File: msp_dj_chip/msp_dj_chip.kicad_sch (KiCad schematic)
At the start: 6 parts, among them U1 DAC60502

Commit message: Add files via upload
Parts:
- removed U1: DAC60502, symbol bernie_symbols:DAC
- added C1, C2: 100nF, symbol Device:C_Small
- added C10, C12, C8, C9: 100n, symbol Device:C_Small
- added C11: 4u7, symbol Device:C_Polarized_Small
- added C13: u1F, symbol Device:C_Small
- added C14: 10uF, symbol Device:C_Small
- added C15: u47, symbol Device:C_Small
- added C16: 10nF, symbol Device:C_Small
- added C17, C18: 15pF, symbol Device:C_Small
- added C3: 150nF, symbol Device:C_Small
- added C4, C5: 10u, symbol Device:C_Small
- added C6, C7: 47p, symbol Device:C_Small
- added D1, D2, D3, D4, D5: LED_Small_Filled, symbol Device:LED_Small_Filled
- added FB1: 600R@100Mhz, symbol Device:FerriteBead_Small
- added J1, J2: Conn_01x04_Pin, symbol Connector:Conn_01x04_Pin
- added J10, J11, J12, J13, J14, J15, J16, J17, J18, J19, J20, J21, J3, J4, J5, J6, J9: Conn_01x02_Socket, symbol Connector:Conn_01x02_Socket
- added J22, J23: Conn_01x06_Socket, symbol Connector:Conn_01x06_Socket
- added J8: Conn_02x05_Odd_Even, symbol Connector_Generic:Conn_02x05_Odd_Even
- added R10, R11, R18: 2K2, symbol Device:R_Small
- added R12, R13: 27R, symbol Device:R_Small
- added R14, R15, R16: 10K, symbol Device:R_Small
- added R17: 330R, symbol Device:R_Small
- added R19, R20: 5K1, symbol Device:R_Small
- added R21, R22: 0R, symbol Device:R_Small
- added R23, R25, R26: 47K, symbol Device:R_Small
- added R24: 100K, symbol Device:R_Small
- added R6, R8, R9: 1K, symbol Device:R_Small
- added R7: 10k, symbol Device:R_Small
- added TP1: TestPoint, symbol Connector:TestPoint
- added U1: ~, symbol Project_Symbols:RS485_THVD2412
- added U2: DAC60502, symbol Project_Symbols:DAC_60502
- added U3: ~, symbol Project_Symbols:OpAmp_NCV272
- added U4: NCP1117-3.3_SOT223, Package_TO_SOT_SMD:SOT-223-3_TabPin2, symbol Regulator_Linear:NCP1117-3.3_SOT223
- added U5: ~, symbol Project_Symbols:ftdi_FT231X
- added U6: ~, symbol Project_Symbols:MCU_MSPM0G3507
- added Y1: Crystal_GND24_Small, symbol Device:Crystal_GND24_Small
- R1: value 1K -> 4K7; footprint Resistor_SMD:R_0603_1608Metric -> (none); now not fitted
- R2: footprint Resistor_SMD:R_0603_1608Metric -> (none)
- R3: footprint Resistor_SMD:R_0603_1608Metric -> (none); now not fitted
- R4, R5: value 1K -> 120R; footprint Resistor_SMD:R_0603_1608Metric -> (none)
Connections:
- net +3V3: now also J1.3 (Pin_3), R17.1; no longer R1.1, R2.1, R3.1, R4.1, R5.1
- net GND: now also C1.2, C10.2, C11.2, C12.2, C13.2, C14.2, C15.2, C16.2, C17.1, C18.1, C2.2, C3.2, C4.2, C5.2, C6.2, C7.2, C8.2, C9.2, D4.1 (K), D5.1 (K), J1.2 (Pin_2), J1.4 (Pin_4), J22.1 (Pin_1), J23.1 (Pin_1), J23.2 (Pin_2), J8.3 (Pin_3), J8.5 (Pin_5), J8.7 (Pin_7), J8.9 (Pin_9), R15.2, R16.2, R19.1, R20.2, R24.1, R6.2, R8.1, R9.1, U1.11 (PAD), U1.5 (GND), U3.4 (VSS), U4.1 (GND), U5.16 (GND), U5.6 (GND); no longer R1.2, R2.2, R4.2, R5.2
- net NSYNC: now also R7.2, U2.7 (NSYNC)
- net RSTSEL: now also U2.3 (RSTSEL)
- net SCLK: now also U2.6 (SCLK)
- net SDIN: now also U2.8 (SDIN)
- net SPI: now also R6.1, U2.5 (SPI)
- new net: D2.2 (A), R16.1
- new net: J8.10 (Pin_10), R22.1
- new net: C3.1, U2.10 (VREFIO)
- new net: C11.1, C12.1, D3.1 (K), FB1.1
- new net: J8.1 (Pin_1), R21.2
- new net: D5.2 (A), R18.2
- new net: R10.1, R8.2, U3.2 (IN-1)
- new net: R11.1, R9.2, U3.6 (IN-2)
- new net: D2.1 (K), U5.10 (CBUS2)
- new net: R12.2, U5.11 (USBDP)
- new net: R13.2, U5.12 (USBDM)
- new net: D1.1 (K), U5.17 (CBUS1)
- new net: D4.2 (A), R17.2
- new net: C6.1, R13.1
- new net: D1.2 (A), R15.1
- new net: C16.1, R23.1, U6.38 (NRST)
- new net: C15.1, U6.32 (VCORE)
- new net: C7.1, R12.1
- new net +24V: J1.1 (Pin_1), J10.2 (Pin_2), J11.2 (Pin_2), J12.2 (Pin_2), J13.2 (Pin_2), J14.2 (Pin_2), J15.2 (Pin_2), J16.2 (Pin_2), J17.2 (Pin_2), J18.2 (Pin_2), J19.2 (Pin_2), J20.2 (Pin_2), J21.2 (Pin_2), J3.2 (Pin_2), J4.2 (Pin_2), J5.2 (Pin_2), J6.2 (Pin_2), R18.1, U3.8 (VDD)
- new net +3.3V: C1.1, C13.1, C14.1, C2.1, C5.1, C8.1, R1.1, R14.1, R2.1, R21.1, R23.2, R25.2, R26.2, R7.1, U1.10 (V_{CC}), U2.1 (VDD), U4.2 (VO), U5.3 (VCCIO), U6.40 (VDD)
- new net ADC_INPUT_0: U6.8 (PA15/A1_0)
- new net ADC_INPUT_1: U6.9 (PA16)
- new net ANALOG_IN0: J2.2 (Pin_2)
- new net ANALOG_IN1: J2.1 (Pin_1)
- new net CC1: J22.5 (Pin_5), R19.2
- new net CC2: J22.4 (Pin_4), R20.1
- new net D: U1.4 (D)
- new net DAC OUT0: R10.2, U3.1 (OUT_1)
- new net DAC OUT1: R11.2, U3.7 (OUT_2)
- new net DAC_OUT0: J2.4 (Pin_4)
- new net DAC_OUT1: J2.3 (Pin_3)
- new net DE: R3.1, U1.3 (DE)
- new net FTDI 3V3: TP1.1, U5.13 (3V3OUT)
- new net FTDI_RX: U6.11 (PA18)
- new net FTDI_TX: U6.10 (PA17)
- new net HFXIN: C17.2, U6.24 (PA23), Y1.1
- new net HFXOUT: C18.2, U6.25 (PA24), Y1.3
- new net OUT_0: J3.1 (Pin_1)
- new net OUT_1: J4.1 (Pin_1)
- new net OUT_10: J15.1 (Pin_1)
- new net OUT_11: J16.1 (Pin_1)
- new net OUT_12: J17.1 (Pin_1)
- new net OUT_13: J18.1 (Pin_1), J19.1 (Pin_1)
- new net OUT_14: J20.1 (Pin_1)
- new net OUT_15: J21.1 (Pin_1)
- new net OUT_2: J5.1 (Pin_1)
- new net OUT_3: J6.1 (Pin_1)
- new net OUT_4: J9.1 (Pin_1)
- new net OUT_5: J10.1 (Pin_1)
- new net OUT_6: J11.1 (Pin_1)
- new net OUT_7: J12.1 (Pin_1)
- new net OUT_8: J13.1 (Pin_1)
- new net OUT_9: J14.1 (Pin_1)
- new net R: R2.2, U1.1 (R)
- new net RE: R1.2, U1.2 (RE)
- new net RS485_RX: R26.1, U6.34 (PA1)
- new net RS485_TX: R25.1, U6.33 (PA_0/FCC_IN)
- new net RX+: J23.3 (Pin_3), R5.1, U1.9 (A)
- new net RX-: J23.4 (Pin_4), R5.2, U1.8 (B)
- new net SOL_OUT_0: U6.1 (PB13)
- new net SOL_OUT_1: U6.2 (PB14)
- new net SOL_OUT_10: U6.18 (PA22)
- new net SOL_OUT_11: U6.19 (PB20)
- new net SOL_OUT_12: U6.20 (PB21)
- new net SOL_OUT_13: U6.21 (PB22)
- new net SOL_OUT_14: U6.22 (PB23)
- new net SOL_OUT_15: U6.23 (PB24)
- new net SOL_OUT_2: U6.3 (PB15)
- new net SOL_OUT_3: U6.4 (PB16)
- new net SOL_OUT_4: U6.5 (PA12/FCC_IN)
- new net SOL_OUT_5: U6.6 (PA13)
- new net SOL_OUT_6: U6.14 (PB17)
- new net SOL_OUT_7: U6.15 (PB18)
- new net SOL_OUT_8: U6.16 (PB19)
- new net SOL_OUT_9: U6.17 (PA21)
- new net SPI_0_CS: R24.2, U6.42 (PA2)
- new net SPI_PICO: U6.7 (PA14/A0_12/CLK_OUT)
- new net SPI_POCI: U6.56 (PA10)
- new net SPI_SCLK: U6.57 (PA11)
- new net SWCLK: U6.13 (PA20)
- new net SWDIO: U6.12 (PA19)
- new net TX+: J23.5 (Pin_5), R4.1, U1.6 (Y)
- new net TX-: J23.6 (Pin_6), R4.2, U1.7 (Z)
- new net UART2 RX: U5.20 (TXD)
- new net UART2 TX: U5.4 (RXD)
- new net USB_D+: J22.2 (Pin_2)
- new net USB_D-: J22.3 (Pin_3)
- new net VBUS: C4.1, D3.2 (A), J22.6 (Pin_6), U4.3 (VI)
- new net VBUS_FILT: C10.1, C9.1, FB1.2, U5.15 (VCC)
- new net VOUTA: U2.2 (VOUTA), U3.3 (IN+1)
- new net VOUTB: U2.9 (VOUTB), U3.5 (IN+2)
- new net nRESET: R22.2, U5.14 (~{RESET})
- no-connect marks 0 -> 10
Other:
- note added: "ANALOGUE OUT"
- note added: "DAC"
- note added: "FTDI"
- note added: "LDO"
- note added: "OP-AMP"
- note added: "POWER + INPUT"
- note added: "PROGRAMMING HEADER"
- note added: "RS485"
- note added: "RS485 OUTPUT"
- note added: "SOL OUT"
- note added: "USB"

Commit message: Add files via upload
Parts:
- added R27, R28: 1R, symbol Device:R_Small
- added R29, R30: 2K2, symbol Device:R_Small
- added R33: 1K, symbol Device:R_Small
- added U8: NCV272DMR2G, symbol Project_Symbols:OpAmp_NCV272
- C1, C10, C12, C2, C3, C6, C7, C8, C9: footprint (none) -> Capacitor_SMD:C_0402_1005Metric
- C4, C5: footprint (none) -> Capacitor_SMD:C_0603_1608Metric
- D1, D2, D3, D4, D5: footprint (none) -> LED_SMD:LED_0603_1608Metric
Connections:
- net ADC_INPUT_0 is gone; now on net VBUS: U6.8 (PA15/A1_0)
- net ADC_INPUT_1 is gone; now on net +24V: U6.9 (PA16)
- net +24V: now also R28.2, U8.8 (VDD)
- net DAC OUT0: now also R29.2, R30.2
- net GND: now also R27.1, R28.1, U8.4 (VSS)
- net VBUS: now also R27.2
- net DAC_0: now reaches U6.54 (PA8)
- net DAC_0: now also R33.1
- new net: R29.1, R33.2, U8.2 (IN-1)
- new net: R30.1, U8.3 (IN+1)
- no-connect marks 10 -> 13
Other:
- note added: "24 Current Sense"
- note added: "VBUS Current Sense"

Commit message: Add files via upload
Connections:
- net DAC OUT0: now also U8.1 (OUT_1)
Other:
- added sheet led-driver (led_driver.kicad_sch)
- added sheet solenoid-driver-boards-dj (solenoid-driver-boards-dj.kicad_sch)

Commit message: Worked on the SOL Driver
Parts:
- U8: footprint (none) -> Package_SO:MSOP-8_3x3mm_P0.65mm
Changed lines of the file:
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@@
 			)
 		)
-		(property "Footprint" ""
+		(property "Footprint" "Package_SO:MSOP-8_3x3mm_P0.65mm"
 			(at 317.5 129.54 0)
 			(effects
@@
 			)
 		)
-		(property "Footprint" ""
+		(property "Footprint" "Package_SO:MSOP-8_3x3mm_P0.65mm"
 			(at 317.5 142.24 0)
 			(effects
@@
 	)
 	(sheet
-		(at 90.17 176.53)
+		(at 86.36 186.69)
 		(size 34.29 48.26)
 		(exclude_from_sim no)
@@
 		)
 		(property "Sheetname" "solenoid-driver-boards-dj"
-			(at 90.17 175.8184 0)
+			(at 86.36 185.9784 0)
 			(effects
 				(font
@@
 		)
 		(property "Sheetfile" "solenoid-driver-boards-dj.kicad_sch"
-			(at 90.17 225.3746 0)
+			(at 86.36 235.5346 0)
 			(effects
 				(font

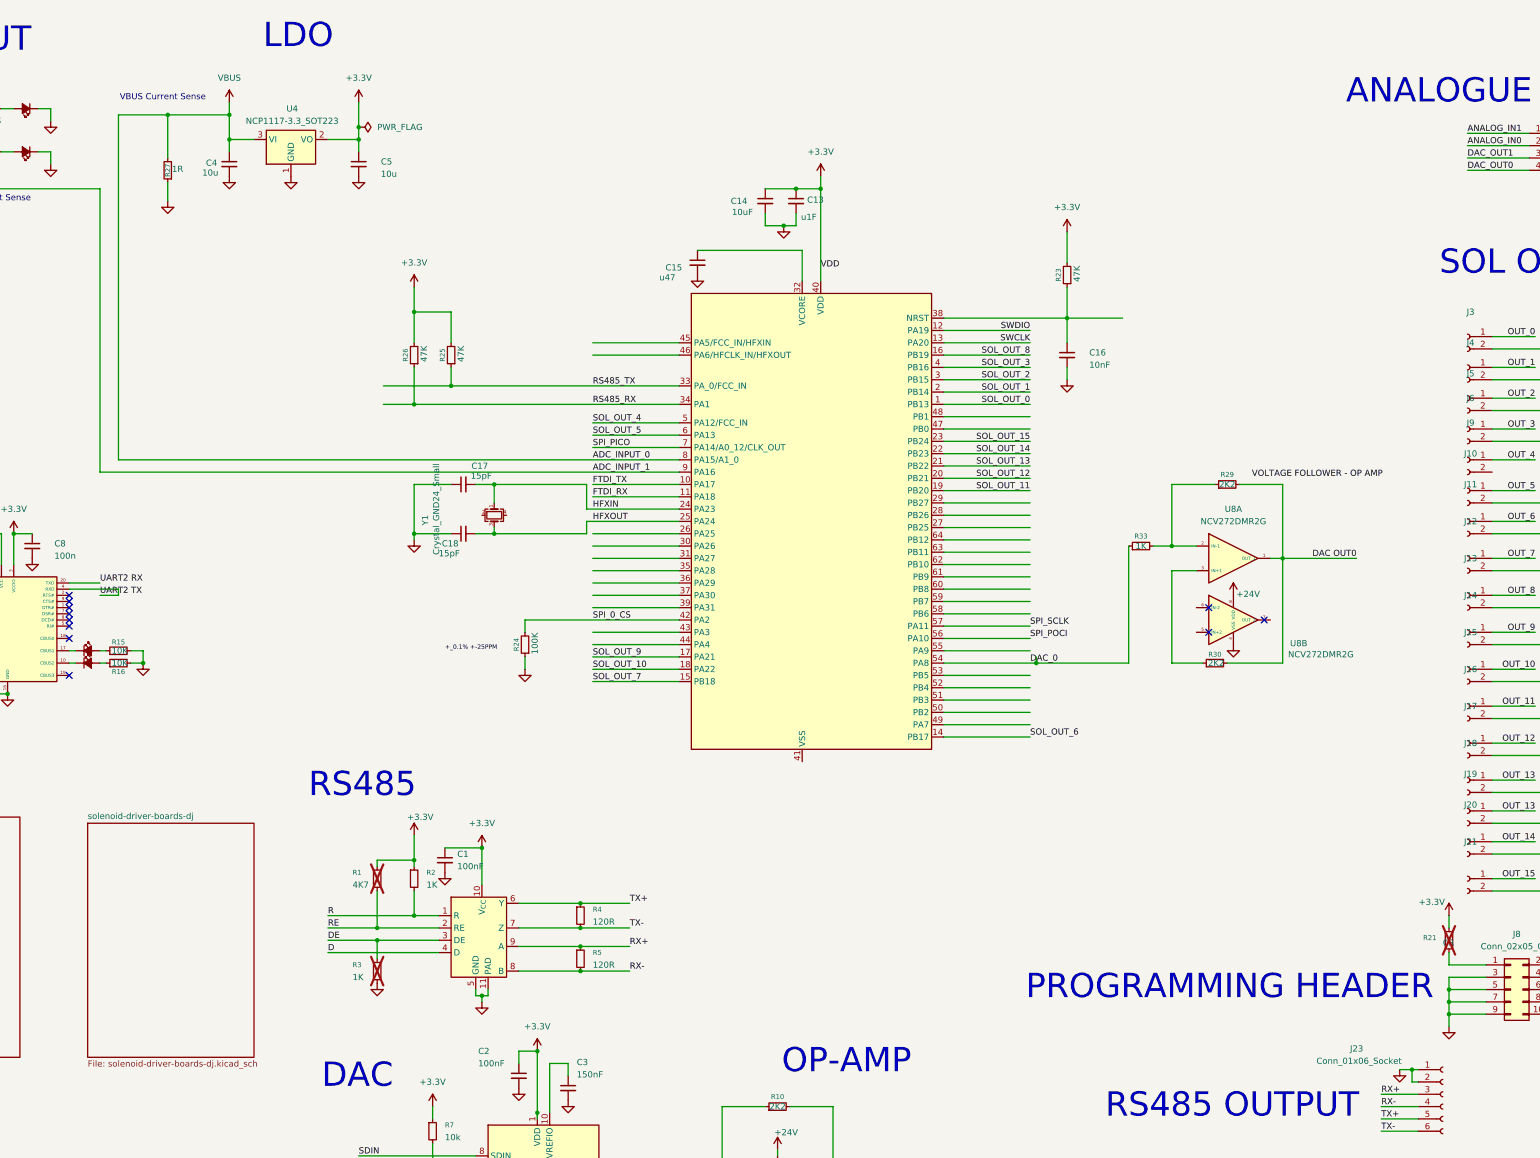
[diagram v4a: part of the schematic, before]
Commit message: pin assignment adjustments - 16 adc
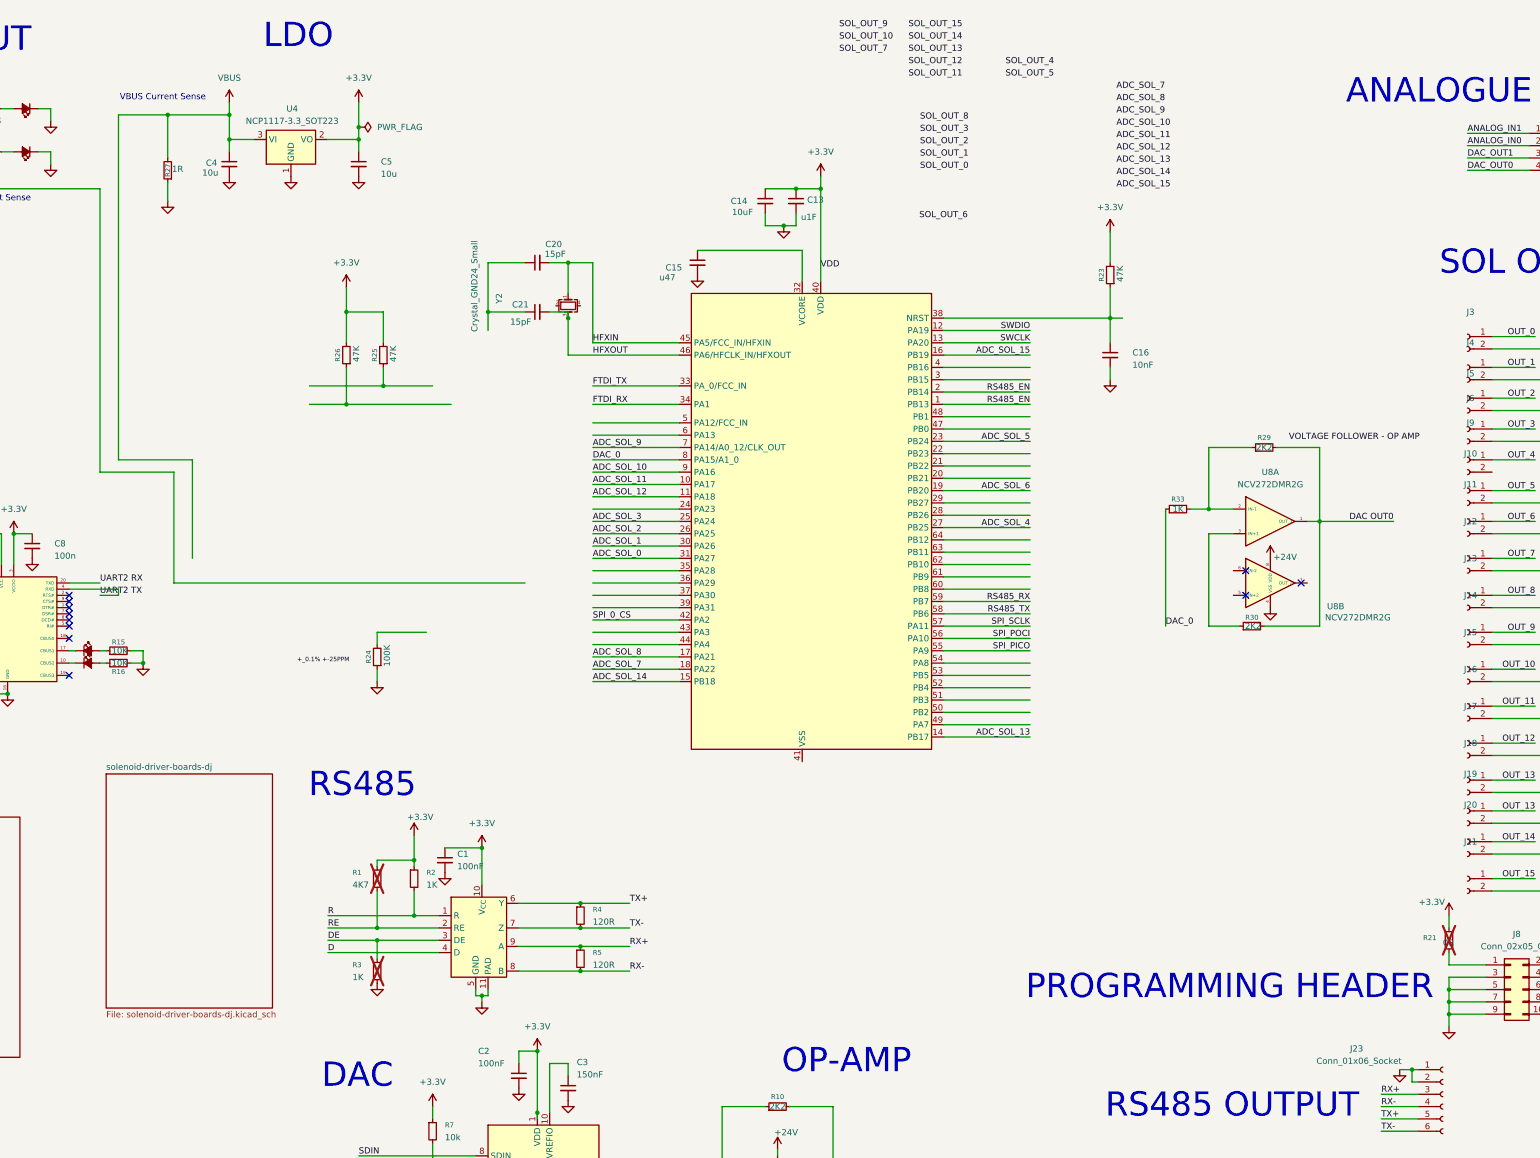
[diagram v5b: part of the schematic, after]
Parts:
- removed C17, C18: 15pF, symbol Device:C_Small
- removed Y1: Crystal_GND24_Small, symbol Device:Crystal_GND24_Small
- added C20, C21: 15pF, symbol Device:C_Small
- added Y2: Crystal_GND24_Small, symbol Device:Crystal_GND24_Small
- U8: footprint Package_SO:MSOP-8_3x3mm_P0.65mm -> (none)
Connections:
- net +24V: no longer U6.9 (PA16)
- net DAC_0: now also U6.8 (PA15/A1_0); no longer U6.54 (PA8)
- net FTDI_RX: now also U6.34 (PA1); no longer U6.11 (PA18)
- net FTDI_TX: now also U6.33 (PA_0/FCC_IN); no longer U6.10 (PA17)
- net HFXIN: now also U6.45 (PA5/FCC_IN/HFXIN), C20.2, Y2.1; no longer U6.24 (PA23)
- net HFXOUT: now also U6.46 (PA6/HFCLK_IN/HFXOUT), C21.2, Y2.3; no longer U6.25 (PA24)
- net RS485_RX: now also U6.59 (PB7); no longer R26.1, U6.34 (PA1)
- net RS485_TX: now also U6.58 (PB6); no longer R25.1, U6.33 (PA_0/FCC_IN)
- net SOL_OUT_0: no longer U6.1 (PB13)
- net SOL_OUT_1: no longer U6.2 (PB14)
- net SOL_OUT_10: no longer U6.18 (PA22)
- net SOL_OUT_11: no longer U6.19 (PB20)
- net SOL_OUT_12: no longer U6.20 (PB21)
- net SOL_OUT_13: no longer U6.21 (PB22)
- net SOL_OUT_14: no longer U6.22 (PB23)
- net SOL_OUT_15: no longer U6.23 (PB24)
- net SOL_OUT_2: no longer U6.3 (PB15)
- net SOL_OUT_3: no longer U6.4 (PB16)
- net SOL_OUT_4: no longer U6.5 (PA12/FCC_IN)
- net SOL_OUT_5: no longer U6.6 (PA13)
- net SOL_OUT_6: no longer U6.14 (PB17)
- net SOL_OUT_7: no longer U6.15 (PB18)
- net SOL_OUT_8: no longer U6.16 (PB19)
- net SOL_OUT_9: no longer U6.17 (PA21)
- net SPI_0_CS: no longer R24.2
- net SPI_PICO: now also U6.55 (PA9); no longer U6.7 (PA14/A0_12/CLK_OUT)
- net VBUS: no longer U6.8 (PA15/A1_0)
- net ADC_SOL_2: now reaches U6.26 (PA25)
- net ADC_SOL_4: now reaches U6.27 (PB25)
- net ADC_SOL_1: now reaches U6.30 (PA26)
- net ADC_SOL_0: now reaches U6.31 (PA27)
- new net: C20.1, C21.1
- new net ADC_SOL_10: U6.9 (PA16)
- new net ADC_SOL_11: U6.10 (PA17)
- new net ADC_SOL_12: U6.11 (PA18)
- new net ADC_SOL_13: U6.14 (PB17)
- new net ADC_SOL_14: U6.15 (PB18)
- new net ADC_SOL_15: U6.16 (PB19)
- new net ADC_SOL_3: U6.25 (PA24)
- new net ADC_SOL_5: U6.23 (PB24)
- new net ADC_SOL_6: U6.19 (PB20)
- new net ADC_SOL_7: U6.18 (PA22)
- new net ADC_SOL_8: U6.17 (PA21)
- new net ADC_SOL_9: U6.7 (PA14/A0_12/CLK_OUT)
- new net RS485_EN: U6.1 (PB13), U6.2 (PB14)
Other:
- moved on the sheet: C16, R23, R24, R25, R26, R29, R30, R33, U8A, U8B
